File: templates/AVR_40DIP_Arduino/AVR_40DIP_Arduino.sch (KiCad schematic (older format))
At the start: 0 parts

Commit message: Wire up 40DIP template.
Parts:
- added C? (x2): 22pF, symbol C
- added C? (x2): 0.1μF, symbol C
- added J?: ISP6, symbol ISP6
- added J?: FTDI_Header, avr-arduino:FTDI_Header, symbol FTDI_Header
- added R?: 10K, symbol R
- added U?: AVR_40DIP_Arduino, Housings_DIP:DIP-40_W15.24mm, symbol AVR_40DIP_Arduino
- added Y?: Crystal, symbol Crystal
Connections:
- new net: C?.1, J?.1 (DTR)
- new net GND: C?.2, C?.2, C?.2, J?.5 (CTS), J?.6 (GND), J?.6 (GND), U?.11 (GND), U?.31 (GND), U?.32 (AREF)
- new net MISO: J?.1 (MISO), U?.7 (PB6/D6(MISO))
- new net MOSI: J?.4 (MOSI), U?.6 (PB5/D5(MOSI))
- new net RX: J?.3 (TX), U?.14 (PD0/D8(RXD0))
- new net SCK: J?.3 (SCK), U?.8 (PB7/D7(SCK))
- new net TX: J?.2 (RX), U?.15 (PD1/D9(TXD0))
- new net VCC: C?.1, J?.2 (VCC), J?.4 (VCC), R?.1, U?.10 (VCC), U?.30 (AVCC)
- new net XTAL1: C?.1, U?.13 (XTAL1), Y?.1
- new net XTAL2: C?.1, U?.12 (XTAL2), Y?.2
- new net ~RESET: C?.2, J?.5 (~RESET), R?.2, U?.9 (~RESET~)
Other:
- note added: "Place as close as possible\nto pins 10 and 11."
- note added: "Place as close as possible\nto pins 12 and 13."

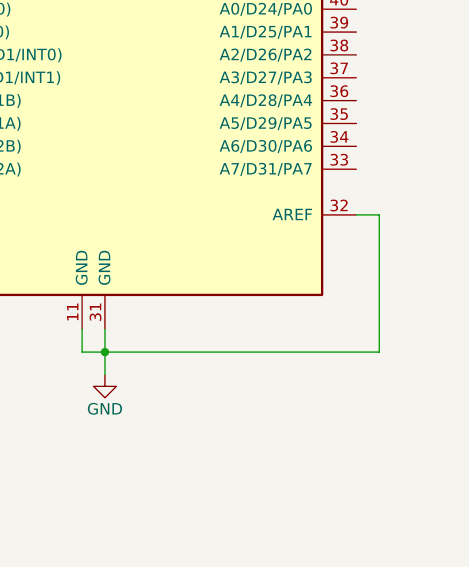
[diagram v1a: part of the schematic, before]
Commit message: Add a capacitor between AREF and GND.  Also, make AREF Passive.
See this discussion:
https://forum.kicad.info/t/barebones-atmega328-circuit-and-the-conflict-between-pins-warning/10886
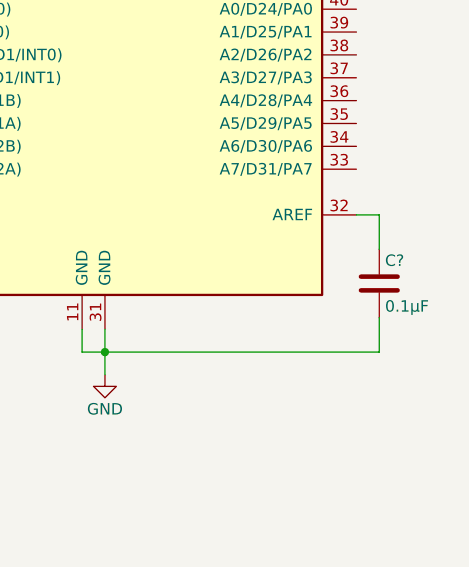
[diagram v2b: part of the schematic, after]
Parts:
- added C?: 0.1μF, symbol C
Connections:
- net GND: now also C?.2; no longer U?.32 (AREF)
- new net: C?.1, U?.32 (AREF)
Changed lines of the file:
@@
 Wire Wire Line
 	6500 4500 6600 4500
-Wire Wire Line
-	6600 4500 6600 5100
 Text Label 4000 3200 0    50   ~ 0
 MOSI
@@
 Wire Notes Line
 	2650 6550 2650 8000
+$Comp
+L C C?
+U 1 1 5B0988E7
+P 6600 4800
+F 0 "C?" H 6625 4900 50  0000 L CNN
+F 1 "0.1μF" H 6625 4700 50  0000 L CNN
+F 2 "" H 6638 4650 50  0001 C CNN
+F 3 "" H 6600 4800 50  0001 C CNN
+	1    6600 4800
+	1    0    0    -1
+$EndComp
+Wire Wire Line
+	6600 4500 6600 4650
+Wire Wire Line
+	6600 5100 6600 4950
 $EndSCHEMATC
